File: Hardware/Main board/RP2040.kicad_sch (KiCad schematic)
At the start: 21 parts, among them J3 Conn_ARM_SWD_TagConnect_TC203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, U10 ABM8-272-T3, U9 RP2040

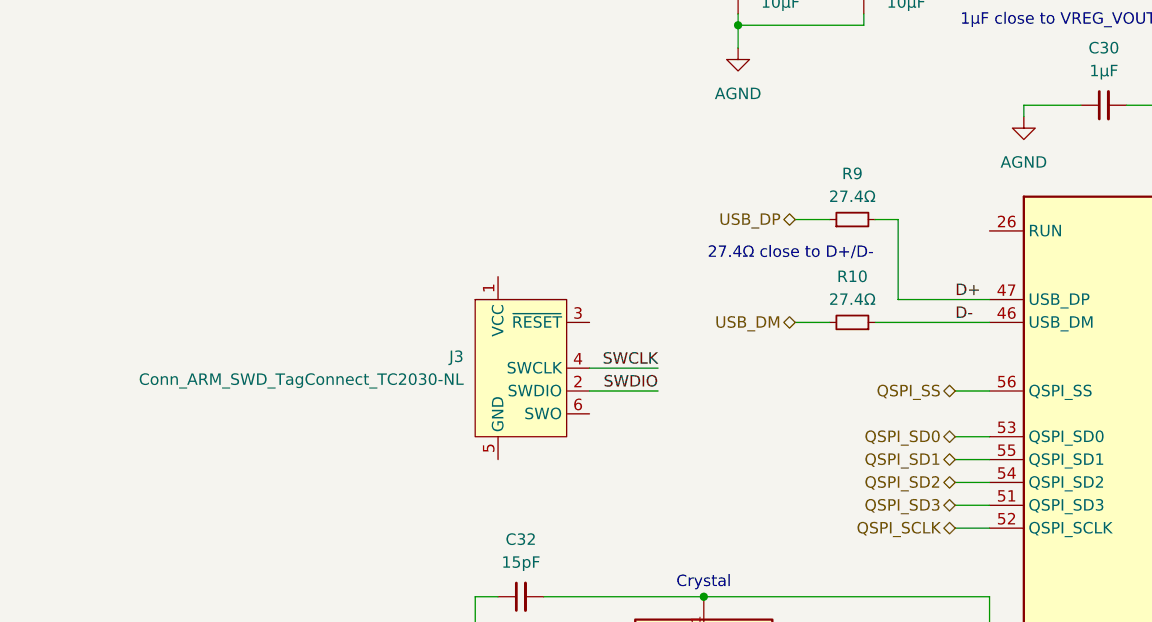
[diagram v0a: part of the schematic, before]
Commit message: Add TagConnect SWD
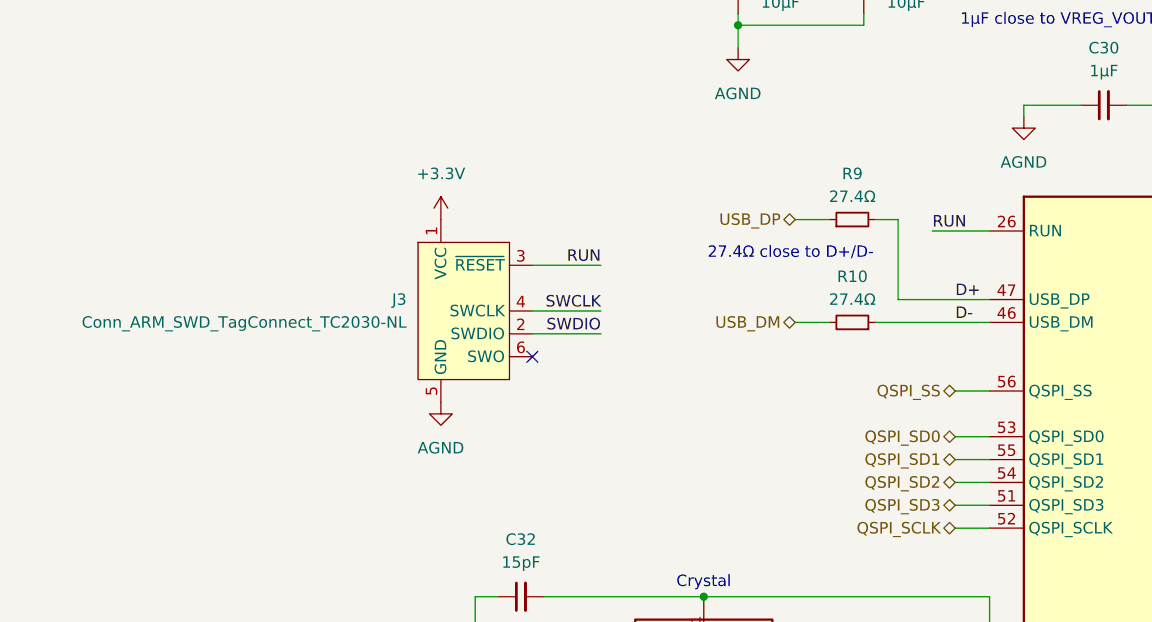
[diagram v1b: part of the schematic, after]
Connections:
- net +3.3V: now also J3.1 (VCC)
- net AGND: now also J3.5 (GND)
- net RUN: now reaches J3.3 (~{RESET})
- net RUN: now also U9.26 (RUN)
- no-connect marks 0 -> 1
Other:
- moved on the sheet: J3
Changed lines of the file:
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@@
 		(color 0 0 0 0)
 	)
+	(no_connect
+		(at 52.07 86.36)
+	)
 	(wire
 		(pts
@@
 	(wire
 		(pts
-			(xy 66.04 90.17) (xy 58.42 90.17)
+			(xy 59.69 83.82) (xy 52.07 83.82)
 		)
 		(stroke
@@
 	(wire
 		(pts
+			(xy 96.52 72.39) (xy 102.87 72.39)
+		)
+		(stroke
+			(width 0)
+			(type default)
+		)
+	)
+	(wire
+		(pts
 			(xy 254 52.07) (xy 254 49.53)
 		)
@@
 	(wire
 		(pts
+			(xy 59.69 76.2) (xy 52.07 76.2)
+		)
+		(stroke
+			(width 0)
+			(type default)
+		)
+	)
+	(wire
+		(pts
 			(xy 74.93 49.53) (xy 88.9 49.53)
 		)
@@
 	(wire
 		(pts
-			(xy 66.04 87.63) (xy 58.42 87.63)
+			(xy 59.69 81.28) (xy 52.07 81.28)
 		)
 		(stroke
@@
 		)
 	)
+	(label "RUN"
+		(at 96.52 72.39 0)
+		(effects
+			(font
+				(size 1.27 1.27)
+			)
+			(justify left bottom)
+		)
+	)
 	(label "SWCLK"
-		(at 66.04 87.63 180)
+		(at 59.69 81.28 180)
 		(effects
 			(font
@@
 	)
 	(label "SWDIO"
-		(at 66.04 90.17 180)
+		(at 59.69 83.82 180)
 		(effects
 			(font
@@
 			)
 			(justify left bottom)
+		)
+	)
+	(label "RUN"
+		(at 59.69 76.2 180)
+		(effects
+			(font
+				(size 1.27 1.27)
+			)
+			(justify right bottom)
 		)
 	)
@@
 	(symbol
 		(lib_id "Connector:Conn_ARM_SWD_TagConnect_TC2030-NL")
-		(at 50.8 87.63 0)
+		(at 44.45 81.28 0)
 		(unit 1)
 		(exclude_from_sim no)
@@
 		(fields_autoplaced yes)
 		(property "Reference" "J3"
-			(at 44.45 86.3599 0)
+			(at 38.1 80.0099 0)
 			(effects
 				(font
@@
 		)
 		(property "Value" "Conn_ARM_SWD_TagConnect_TC2030-NL"
-			(at 44.45 88.8999 0)
+			(at 38.1 82.5499 0)
 			(effects
 				(font
@@
 		)
 		(property "Footprint" "Connector:Tag-Connect_TC2030-IDC-NL_2x03_P1.27mm_Vertical"
-			(at 50.8 105.41 0)
+			(at 44.45 99.06 0)
 			(effects
 				(font
@@
 		)
 		(property "Datasheet" "https://www.tag-connect.com/wp-content/uploads/bsk-pdf-manager/TC2030-CTX_1.pdf"
-			(at 50.8 102.87 0)
+			(at 44.45 96.52 0)
 			(effects
 				(font
@@
 		)
 		(property "Description" "Tag-Connect ARM Cortex SWD JTAG connector, 6 pin, no legs"
-			(at 50.8 87.63 0)
+			(at 44.45 81.28 0)
 			(effects
 				(font
@@
 				(path "/e5119d15-74fb-4259-abbc-5cab1f368532/9c03ac80-c552-4a59-83c4-4e8b67a63031"
 					(reference "#PWR040")
+					(unit 1)
+				)
+			)
+		)
+	)
+	(symbol
+		(lib_id "power:+3.3V")
+		(at 41.91 71.12 0)
+		(unit 1)
+		(exclude_from_sim no)
+		(in_bom yes)
+		(on_board yes)
+		(dnp no)
+		(fields_autoplaced yes)
+		(property "Reference" "#PWR013"
+			(at 41.91 74.93 0)
+			(effects
+				(font
+					(size 1.27 1.27)
+				)
+				(hide yes)
+			)
+		)
+		(property "Value" "+3.3V"
+			(at 41.91 66.04 0)
+			(effects
+				(font
+					(size 1.27 1.27)
+				)
+			)
+		)
+		(property "Footprint" ""
+			(at 41.91 71.12 0)
+			(effects
+				(font
+					(size 1.27 1.27)
+				)
+				(hide yes)
+			)
+		)
+		(property "Datasheet" ""
+			(at 41.91 71.12 0)
+			(effects
+				(font
+					(size 1.27 1.27)
+				)
+				(hide yes)
+			)
+		)
+		(property "Description" "Power symbol creates a global label with name \"+3.3V\""
+			(at 41.91 71.12 0)
+			(effects
+				(font
+					(size 1.27 1.27)
+				)
+				(hide yes)
+			)
+		)
+		(pin "1"
+		)
+		(instances
+			(project "Display main board"
+				(path "/e5119d15-74fb-4259-abbc-5cab1f368532/9c03ac80-c552-4a59-83c4-4e8b67a63031"
+					(reference "#PWR013")
 					(unit 1)
 				)
@@
 					(unit 1)
 				)
+			)
+		)
+	)
+	(symbol
+		(lib_id "BQ25895-accurate:AGND")
+		(at 41.91 91.44 0)
+		(unit 1)
+		(exclude_from_sim no)
+		(in_bom no)
+		(on_board no)
+		(dnp no)
+		(fields_autoplaced yes)
+		(property "Reference" "#PWR049"
+			(at 41.656 91.44 0)
+			(effects
+				(font
+					(size 1.27 1.27)
+				)
+				(hide yes)
+			)
+		)
+		(property "Value" "AGND"
+			(at 41.91 96.52 0)
+			(effects
+				(font
+					(size 1.27 1.27)
+				)
+			)
+		)
+		(property "Footprint" ""
+			(at 41.91 91.44 0)
+			(effects
+				(font
+					(size 1.27 1.27)
+				)
+				(hide yes)
+			)
+		)
+		(property "Datasheet" ""
+			(at 41.91 91.44 0)
+			(effects
+				(font
+					(size 1.27 1.27)
+				)
+				(hide yes)
+			)
+		)
+		(property "Description" ""
+			(at 41.91 91.44 0)
+			(effects
+				(font
+					(size 1.27 1.27)
+				)
+				(hide yes)
+			)
+		)
+		(pin "1"
+		)
+		(instances
+			(project "Display main board"
+				(path "/e5119d15-74fb-4259-abbc-5cab1f368532/9c03ac80-c552-4a59-83c4-4e8b67a63031"
+					(reference "#PWR049")
+					(unit 1)
+				)

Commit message: add PawConnect
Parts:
- J3: footprint Connector:Tag-Connect_TC2030-IDC-NL_2x03_P1.27mm_Vertical -> PawConnect:Paw-Connect_RevA_TC2030-IDC-NL_2x03_P1.27mm_Vertical
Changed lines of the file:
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@@
 			)
 		)
-		(property "Footprint" "Connector:Tag-Connect_TC2030-IDC-NL_2x03_P1.27mm_Vertical"
+		(property "Footprint" "PawConnect:Paw-Connect_RevA_TC2030-IDC-NL_2x03_P1.27mm_Vertical"
 			(at 44.45 99.06 0)
 			(effects

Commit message: swap PawConnect header
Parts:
- J3: footprint PawConnect:Paw-Connect_RevA_TC2030-IDC-NL_2x03_P1.27mm_Vertical -> PawConnect:Paw-Connect_RevB_TC2030-IDC-NL_2x03_P1.27mm_Vertical
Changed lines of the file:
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@@
 			)
 		)
-		(property "Footprint" "PawConnect:Paw-Connect_RevA_TC2030-IDC-NL_2x03_P1.27mm_Vertical"
+		(property "Footprint" "PawConnect:Paw-Connect_RevB_TC2030-IDC-NL_2x03_P1.27mm_Vertical"
 			(at 44.45 99.06 0)
 			(effects

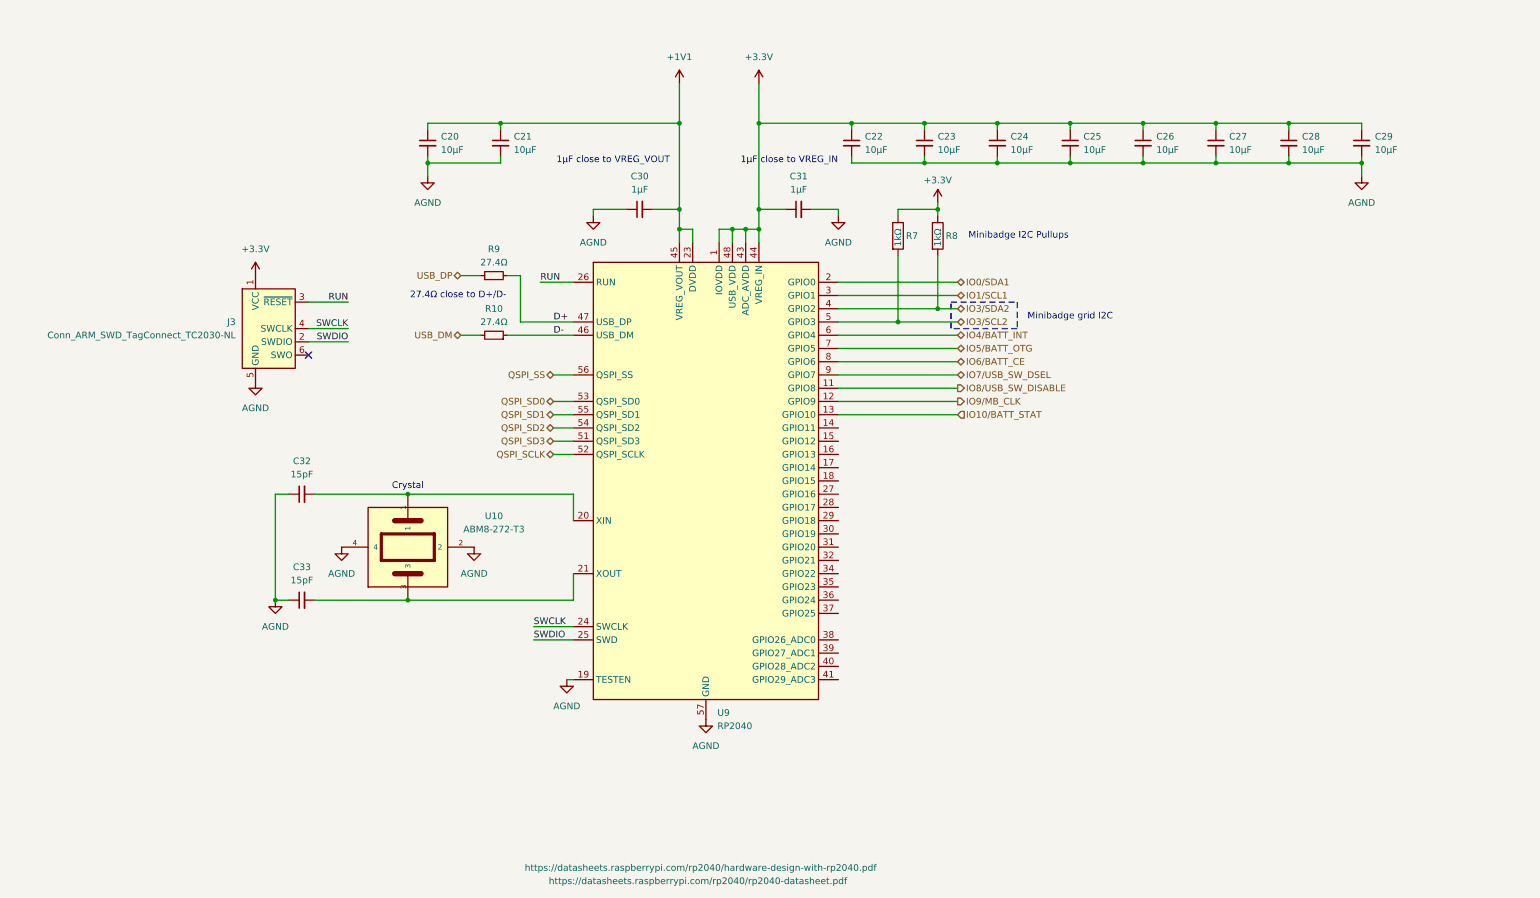
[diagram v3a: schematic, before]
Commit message: Add button and LEDs
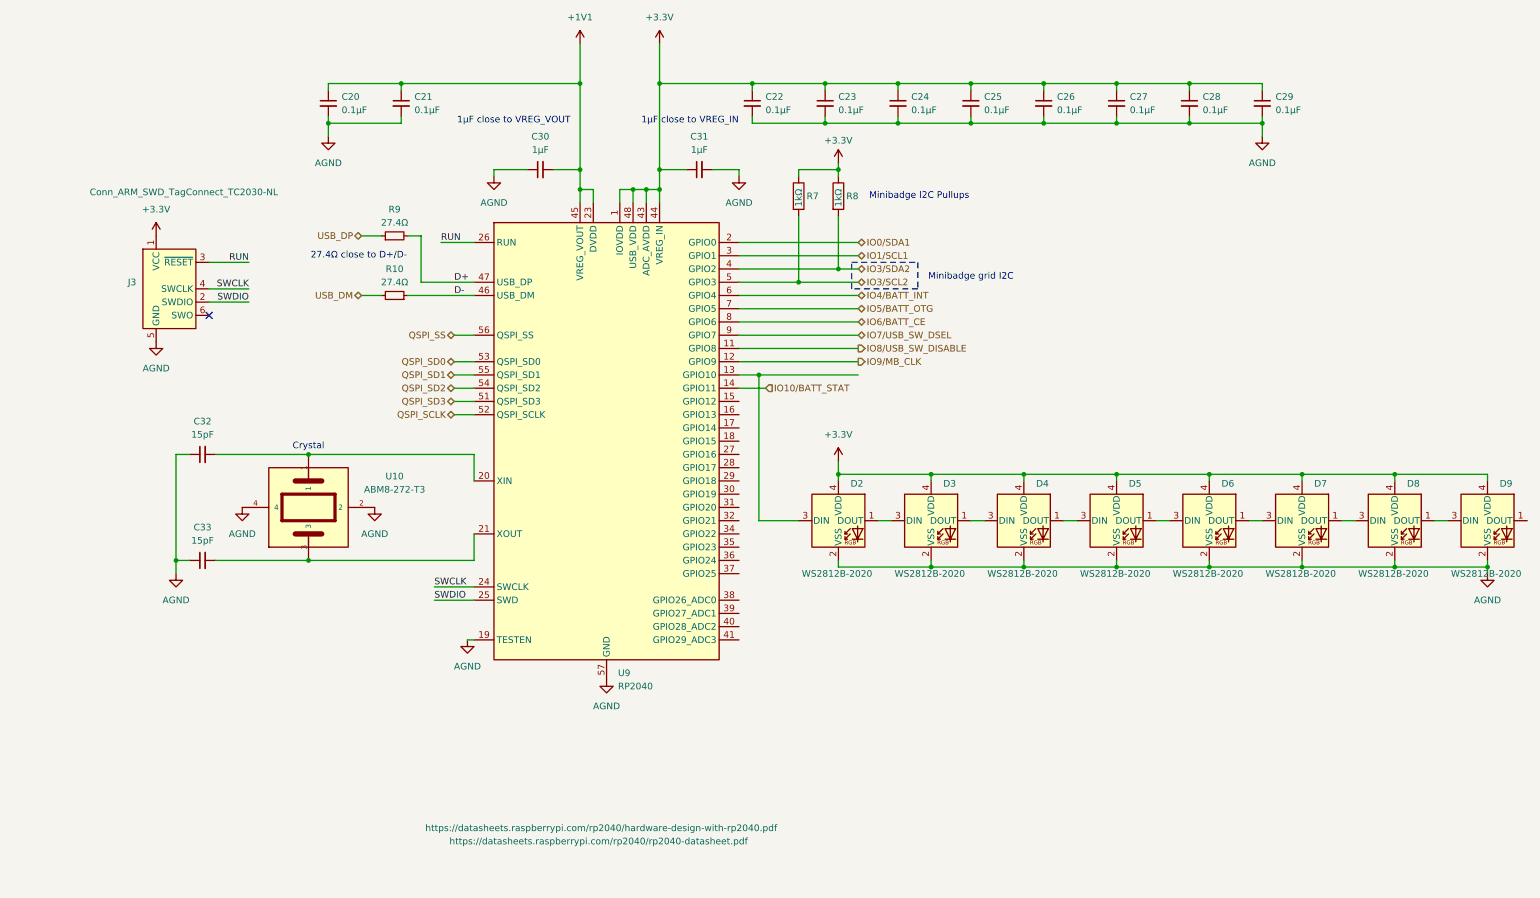
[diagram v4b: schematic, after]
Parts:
- added D2, D3, D4, D5, D6, D7, D8, D9: WS2812B-2020, Library:LED_WS2812B-2020_PLCC4_2.0x2.0mm, symbol LED:WS2812B-2020
- C20, C21, C22, C23, C24, C25, C26, C27, C28, C29: value 10µF -> 0.1µF
- U9: Design guide (none) -> https://datasheets.raspberrypi.com/rp2040/hardware-design-w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
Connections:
- net +3.3V: now also D2.4 (VDD), D3.4 (VDD), D4.4 (VDD), D5.4 (VDD), D6.4 (VDD), D7.4 (VDD), D8.4 (VDD), D9.4 (VDD)
- net AGND: now also D2.2 (VSS), D3.2 (VSS), D4.2 (VSS), D5.2 (VSS), D6.2 (VSS), D7.2 (VSS), D8.2 (VSS), D9.2 (VSS)
- net IO10/BATT_STAT: now also U9.14 (GPIO11); no longer U9.13 (GPIO10)
- new net: D5.1 (DOUT), D6.3 (DIN)
- new net: D4.1 (DOUT), D5.3 (DIN)
- new net: D6.1 (DOUT), D7.3 (DIN)
- new net: D2.3 (DIN), U9.13 (GPIO10)
- new net: D3.1 (DOUT), D4.3 (DIN)
- new net: D2.1 (DOUT), D3.3 (DIN)
- new net: D8.1 (DOUT), D9.3 (DIN)
- new net: D7.1 (DOUT), D8.3 (DIN)
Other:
- moved on the sheet: C20, C21, C22, C23, C24, C25, C26, C27, C28, C29, C30, C31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

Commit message: update constraints
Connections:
- net at U9.13 (GPIO10): no longer D2.3 (DIN)
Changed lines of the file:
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@@
-	)
-	(junction
-		(at 138.43 90.17)
-		(diameter 0)
-		(color 0 0 0 0)
 	)
 	(junction
@@
 	(wire
 		(pts
-			(xy 134.62 90.17) (xy 138.43 90.17)
+			(xy 134.62 90.17) (xy 157.48 90.17)
 		)
 		(stroke
@@
 	(wire
 		(pts
-			(xy 138.43 90.17) (xy 157.48 90.17)
-		)
-		(stroke
-			(width 0)
-			(type default)
-		)
-	)
-	(wire
-		(pts
 			(xy 80.01 92.71) (xy 83.82 92.71)
 		)
@@
 	(wire
 		(pts
-			(xy 138.43 118.11) (xy 146.05 118.11)
-		)
-		(stroke
-			(width 0)
-			(type default)
-		)
-	)
-	(wire
-		(pts
 			(xy 234.95 34.29) (xy 234.95 35.56)
 		)
@@
 	(wire
 		(pts
+			(xy 139.7 118.11) (xy 146.05 118.11)
+		)
+		(stroke
+			(width 0)
+			(type default)
+		)
+	)
+	(wire
+		(pts
 			(xy 116.84 54.61) (xy 119.38 54.61)
 		)
@@
 		)
 		(stroke
-			(width 0)
-			(type default)
-		)
-	)
-	(wire
-		(pts
-			(xy 138.43 90.17) (xy 138.43 118.11)
-		)
-		(stroke

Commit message: fix nets
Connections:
- net at U9.13 (GPIO10): now also D2.3 (DIN)
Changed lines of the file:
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@@
+	(wire
+		(pts
+			(xy 146.05 99.06) (xy 146.05 118.11)
+		)
+		(stroke
+			(width 0)
+			(type default)
+		)
+	)
 	(wire
 		(pts
@@
 	(wire
 		(pts
+			(xy 157.48 99.06) (xy 146.05 99.06)
+		)
+		(stroke
+			(width 0)
+			(type default)
+		)
+	)
+	(wire
+		(pts
 			(xy 134.62 90.17) (xy 157.48 90.17)
 		)
@@
 	(wire
 		(pts
+			(xy 157.48 90.17) (xy 157.48 99.06)
+		)
+		(stroke
+			(width 0)
+			(type default)
+		)
+	)
+	(wire
+		(pts
 			(xy 137.16 41.91) (xy 151.13 41.91)
 		)
@@
 		)
 		(stroke
-			(width 0)
-			(type default)
-		)
-	)
-	(wire
-		(pts
-			(xy 139.7 118.11) (xy 146.05 118.11)
-		)
-		(stroke

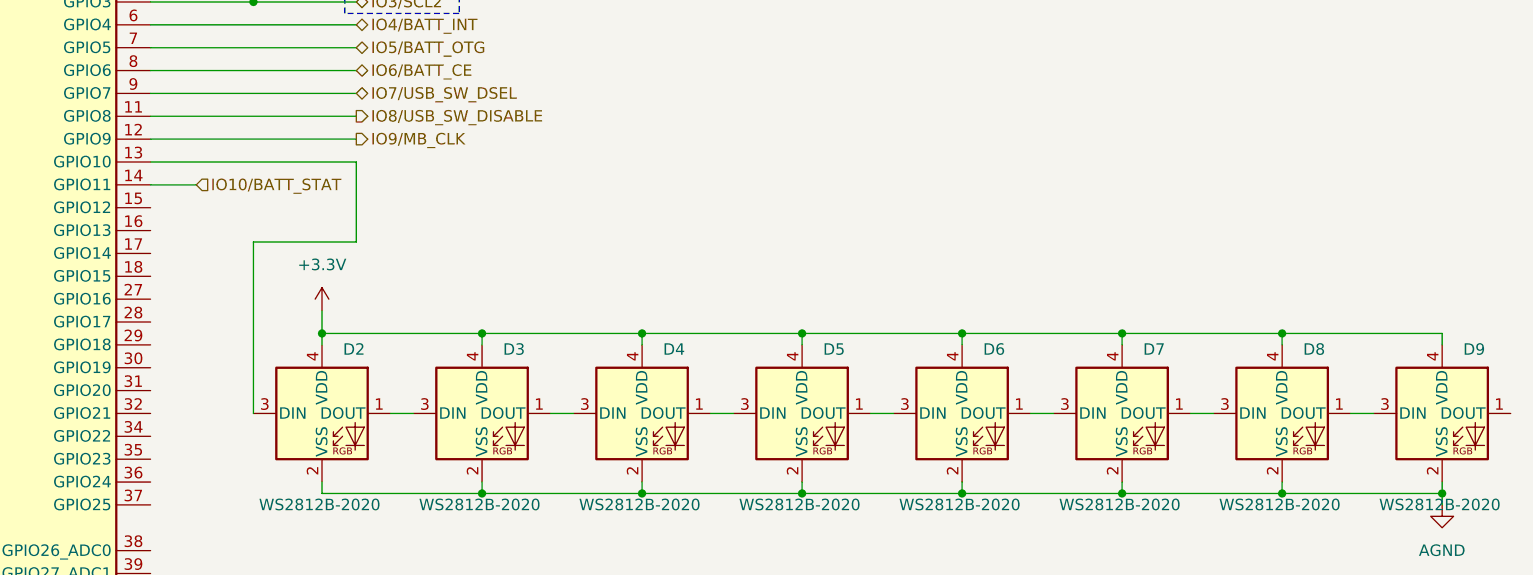
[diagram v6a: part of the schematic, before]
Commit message: add caps for LEDs
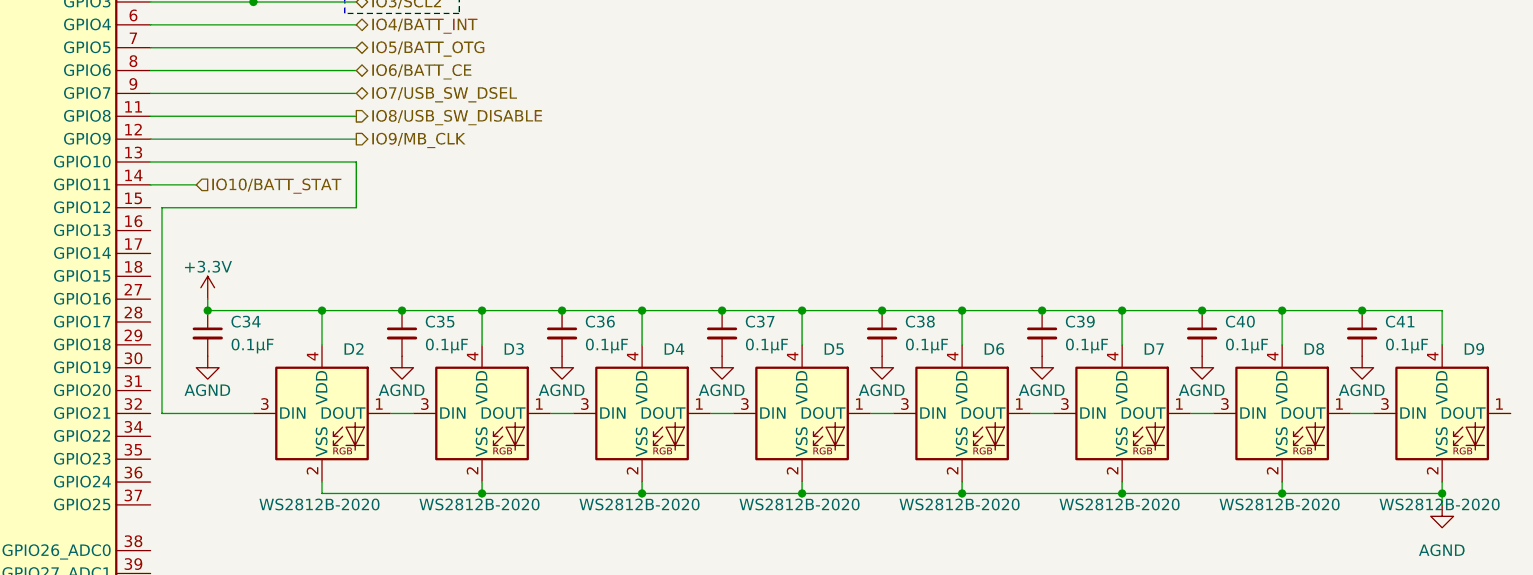
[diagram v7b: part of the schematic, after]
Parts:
- added C34, C35, C36, C37, C38, C39, C40, C41: 0.1μF, Capacitor_SMD:C_0402_1005Metric, symbol Device:C_Small
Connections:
- net +3.3V: now also C34.1, C35.1, C36.1, C37.1, C38.1, C39.1, C40.1, C41.1
- net AGND: now also C34.2, C35.2, C36.2, C37.2, C38.2, C39.2, C40.2, C41.2

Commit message: update footprints
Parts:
- C20, C21, C22, C23, C24, C25, C26, C27, C28, C29: footprint Capacitor_SMD:C_0603_1608Metric -> Capacitor_SMD:C_0402_1005Metric
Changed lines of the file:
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@@
 			)
 		)
-		(property "Footprint" "Capacitor_SMD:C_0603_1608Metric"
+		(property "Footprint" "Capacitor_SMD:C_0402_1005Metric"
 			(at 69.85 38.1 0)
 			(effects
@@
 			)
 		)
-		(property "Footprint" "Capacitor_SMD:C_0603_1608Metric"
+		(property "Footprint" "Capacitor_SMD:C_0402_1005Metric"
 			(at 151.13 38.1 0)
 			(effects
@@
 			)
 		)
-		(property "Footprint" "Capacitor_SMD:C_0603_1608Metric"
+		(property "Footprint" "Capacitor_SMD:C_0402_1005Metric"
 			(at 179.07 38.1 0)
 			(effects
@@
 			)
 		)
-		(property "Footprint" "Capacitor_SMD:C_0603_1608Metric"
+		(property "Footprint" "Capacitor_SMD:C_0402_1005Metric"
 			(at 137.16 38.1 0)
 			(effects
@@
 			)
 		)
-		(property "Footprint" "Capacitor_SMD:C_0603_1608Metric"
+		(property "Footprint" "Capacitor_SMD:C_0402_1005Metric"
 			(at 165.1 38.1 0)
 			(effects
@@
 			)
 		)
-		(property "Footprint" "Capacitor_SMD:C_0603_1608Metric"
+		(property "Footprint" "Capacitor_SMD:C_0402_1005Metric"
 			(at 234.95 38.1 0)
 			(effects
@@
 			)
 		)
-		(property "Footprint" "Capacitor_SMD:C_0603_1608Metric"
+		(property "Footprint" "Capacitor_SMD:C_0402_1005Metric"
 			(at 55.88 38.1 0)
 			(effects
@@
 			)
 		)
-		(property "Footprint" "Capacitor_SMD:C_0603_1608Metric"
+		(property "Footprint" "Capacitor_SMD:C_0402_1005Metric"
 			(at 220.98 38.1 0)
 			(effects
@@
 			)
 		)
-		(property "Footprint" "Capacitor_SMD:C_0603_1608Metric"
+		(property "Footprint" "Capacitor_SMD:C_0402_1005Metric"
 			(at 207.01 38.1 0)
 			(effects
@@
 			)
 		)
-		(property "Footprint" "Capacitor_SMD:C_0603_1608Metric"
+		(property "Footprint" "Capacitor_SMD:C_0402_1005Metric"
 			(at 193.04 38.1 0)
 			(effects
